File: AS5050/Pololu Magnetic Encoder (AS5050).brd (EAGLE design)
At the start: 17.8 x 11.7 mm, 9 parts, among them U1 AS5035

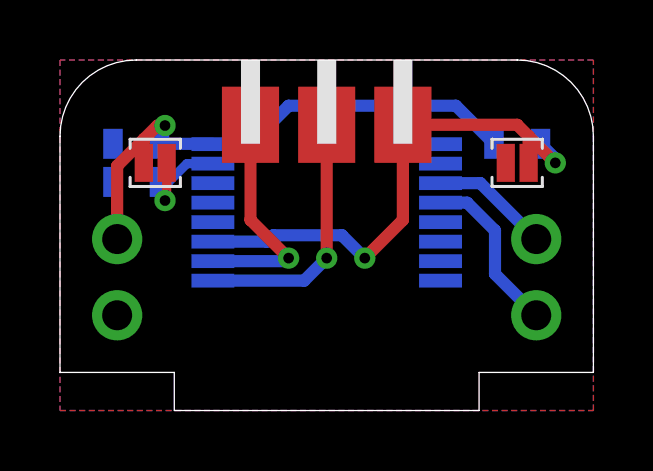
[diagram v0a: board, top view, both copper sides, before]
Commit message: Created and completed AS5050 Encoder PCB
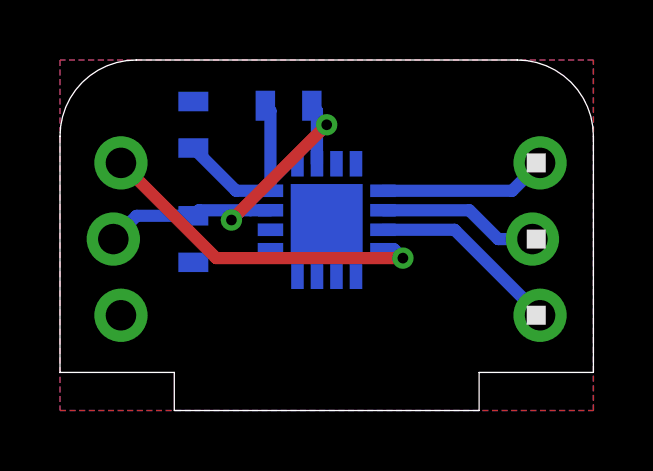
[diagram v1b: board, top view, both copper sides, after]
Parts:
- removed J1, J2: (no value), .solderjumper:2.LRG.PASTE
- removed JP1, JP2: (no value), microbuilder:1X02_ROUND
- removed U$9: 1X3.SIDE, .standardheaders:1X3.SIDE
- added U$4, U$5: 1X3.LOCK, headers(.1in):1X3.LOCK
- C1: value .1uF -> 1uF; device .standardparts:0603 -> standardparts:0603
- C2: value 2.2uF -> 4.7uF; device .standardparts:0603 -> standardparts:0603
- R1: value 100k -> 15; device .standardparts:0603 -> standardparts:0603
- U1: value AS5035 -> AS5050.QFN; device austriamicrosystems:SSOP16 -> austriamicrosystems:QFN.16
- moved R1 7.73 mm to (7.62, 10.2), turned to 0 degrees
- moved C1 3.70 mm to (4.45, 5.71), turned to 270 degrees
- moved C2 2.69 mm to (4.45, 9.53), turned to 270 degrees
- moved U1 0.25 mm to (8.89, 6.35), turned to 0 degrees
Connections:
- removed net A: JP2.2, U1.3
- removed net B: JP2.1, U1.4
- removed net CLK: U$9.1, U1.10
- removed net DO: U$9.2, U1.9
- removed net N$4: C2.1, J1.1, U1.15
- removed net VIN: C1.1, J1.2, JP1.2, R1.1, U1.16
- new net 3.3V: C1.1, R1.1, U$4.2, U1.11, U1.14
- new net MISO: U$5.2, U1.2
- new net MOSI: U$5.3, U1.1
- new net N$1: C2.2, R1.2, U1.12
- new net SCLK: U$5.1, U1.3
- net !CS: now also U$4.1, U1.4; no longer J2.2, R1.2, U$9.3, U1.11
- net GND: now also C2.1, U$4.3, U1.10, U1.13, U1.9; no longer C2.2, J2.1, JP1.1, U1.7
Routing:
- net VIN: track 18.3 -> 0.00 mm, vias 1 -> 0
- net 3.3V: track 0.00 -> 14.0 mm, vias 0 -> 2
- net DO: track 8.55 -> 0.00 mm, vias 1 -> 0
- net CLK: track 8.17 -> 0.00 mm, vias 1 -> 0
- net SCLK: track 0.00 -> 6.42 mm
- net !CS: track 17.8 -> 11.5 mm, vias 2 -> 1
- net N$1: track 0.00 -> 6.07 mm
- net MOSI: track 0.00 -> 5.62 mm
- net B: track 5.59 -> 0.00 mm
- net MISO: track 0.00 -> 5.38 mm
- net N$4: track 4.01 -> 0.00 mm, vias 1 -> 0
- net A: track 3.96 -> 0.00 mm
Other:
- board text added: "AnomalousMaker.com"
- board text added: "GND"
- board text added: "MISO"
- board text added: "MOSI"
- board text added: "SCLK"
- board text removed: "!SPI"
- board text removed: "innovativemaker.com"
